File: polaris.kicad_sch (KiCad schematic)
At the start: 22 parts, among them J101 XT60-M, J102 Screw_Terminal_01x02, J103 Screw_Terminal_01x02, J104 Screw_Terminal_01x02, J105 Screw_Terminal_01x02, J106 Screw_Terminal_01x02, J107 Screw_Terminal_01x02, J108 Screw_Terminal_01x03, J109 Screw_Terminal_01x03, J110 Screw_Terminal_01x03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

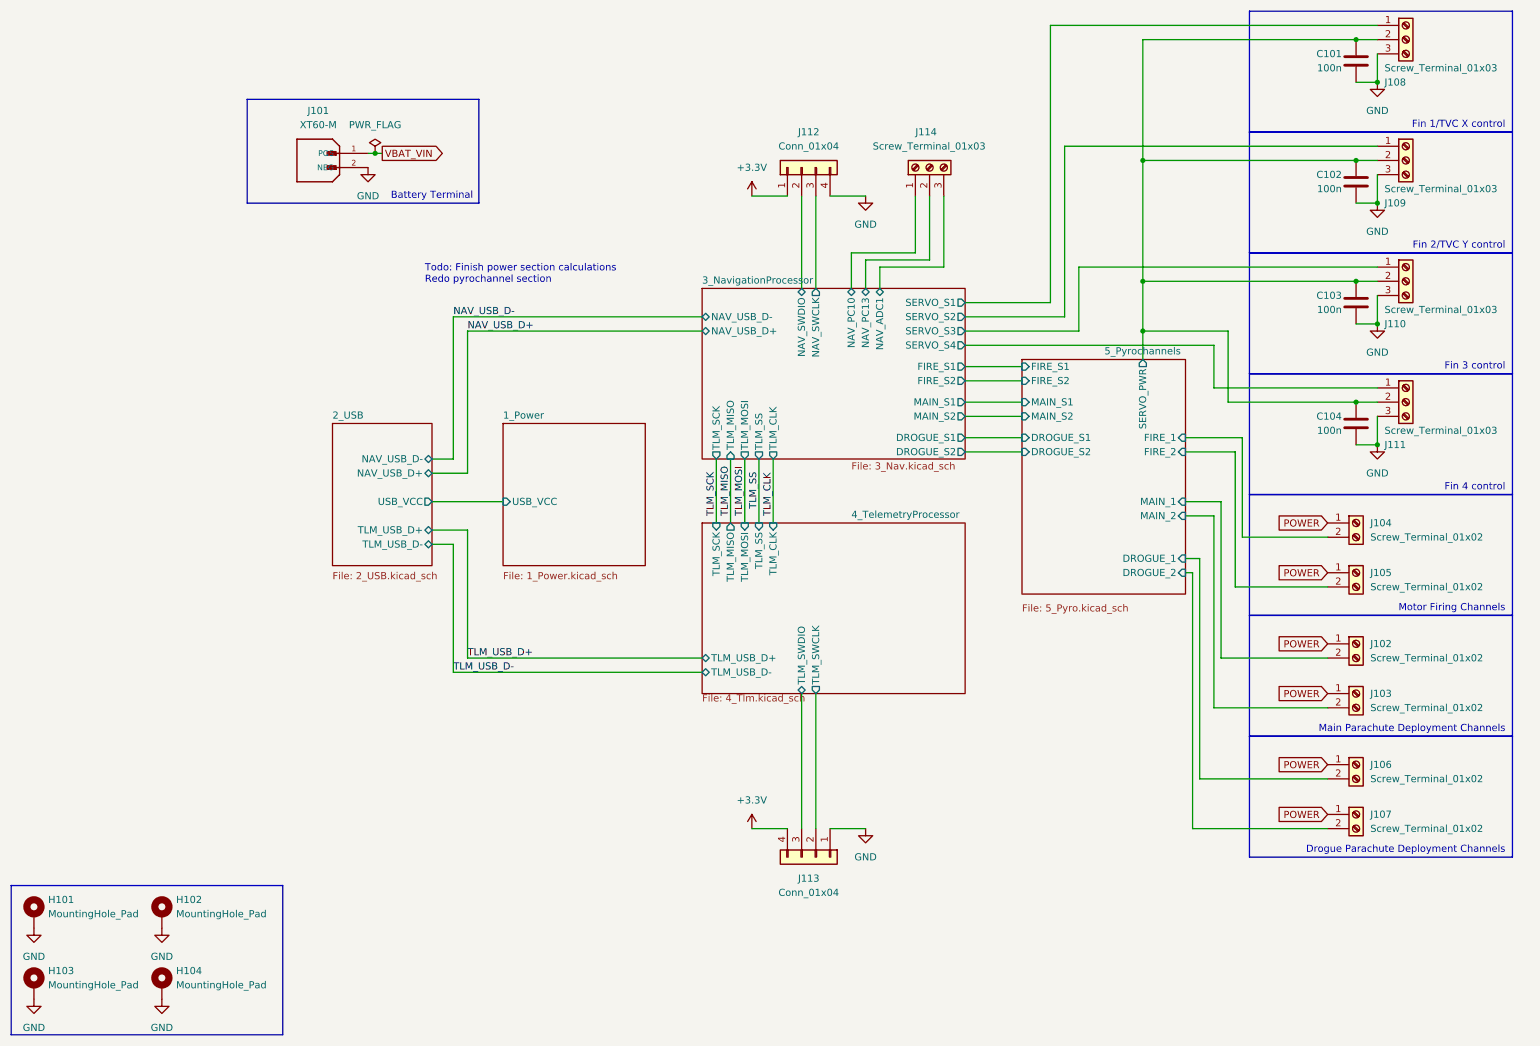
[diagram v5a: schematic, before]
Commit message: Renamed a few nets
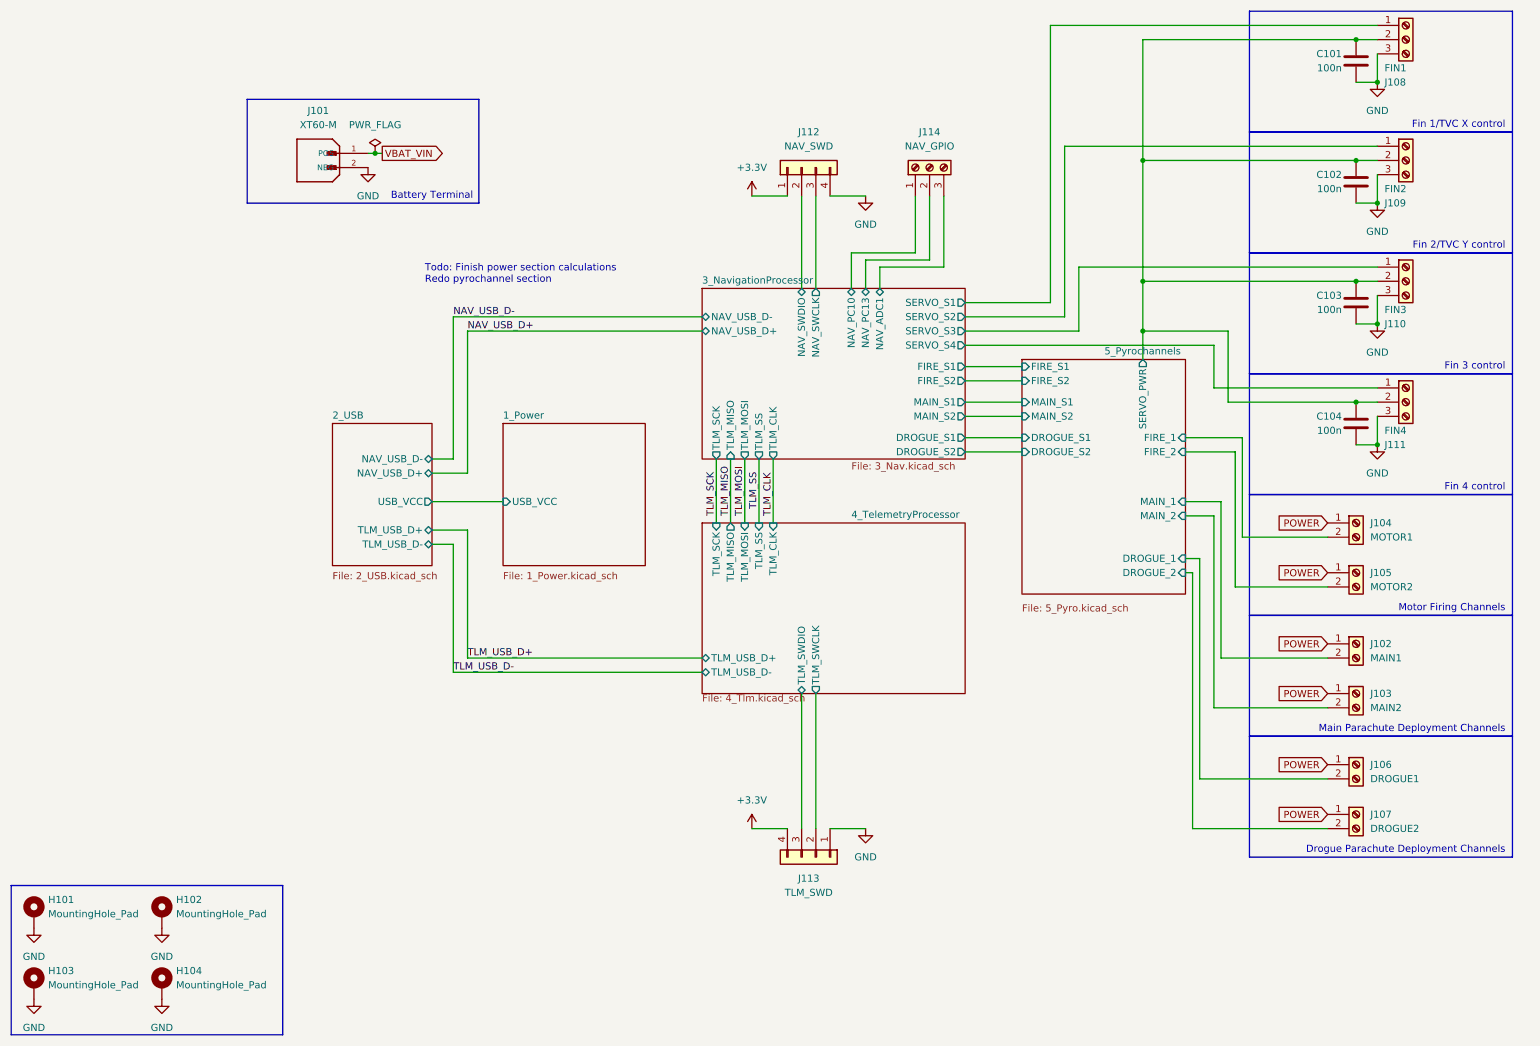
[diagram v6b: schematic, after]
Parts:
- J102: value Screw_Terminal_01x02 -> MAIN1
- J103: value Screw_Terminal_01x02 -> MAIN2
- J104: value Screw_Terminal_01x02 -> MOTOR1
- J105: value Screw_Terminal_01x02 -> MOTOR2
- J106: value Screw_Terminal_01x02 -> DROGUE1
- J107: value Screw_Terminal_01x02 -> DROGUE2
- J108: value Screw_Terminal_01x03 -> FIN1
- J109: value Screw_Terminal_01x03 -> FIN2
- J110: value Screw_Terminal_01x03 -> FIN3
- J111: value Screw_Terminal_01x03 -> FIN4
- J112: value Conn_01x04 -> NAV_SWD
- J113: value Conn_01x04 -> TLM_SWD
- J114: value Screw_Terminal_01x03 -> NAV_GPIO
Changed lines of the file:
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@@
 			)
 		)
-		(property "Value" "Screw_Terminal_01x03"
+		(property "Value" "FIN2"
 			(at 259.08 45.72 0)
 			(show_name no)
@@
 			)
 		)
-		(property "Value" "Screw_Terminal_01x02"
+		(property "Value" "DROGUE2"
 			(at 256.54 160.0199 0)
 			(show_name no)
@@
 			)
 		)
-		(property "Value" "Screw_Terminal_01x03"
+		(property "Value" "FIN3"
 			(at 259.08 67.31 0)
 			(show_name no)
@@
 			)
 		)
-		(property "Value" "Conn_01x04"
+		(property "Value" "NAV_SWD"
 			(at 156.21 38.1 90)
 			(show_name no)
@@
 			)
 		)
-		(property "Value" "Screw_Terminal_01x03"
+		(property "Value" "FIN1"
 			(at 259.08 24.13 0)
 			(show_name no)
@@
 			)
 		)
-		(property "Value" "Screw_Terminal_01x03"
+		(property "Value" "FIN4"
 			(at 259.08 88.9 0)
 			(show_name no)
@@
 		(dnp no)
 		(property "Reference" "J114"
-			(at 175.26 35.56 90)
+			(at 177.8 35.56 90)
 			(show_name no)
 			(do_not_autoplace no)
@@
 					(size 1.27 1.27)
 				)
-				(justify right)
 			)
 		)
-		(property "Value" "Screw_Terminal_01x03"
-			(at 167.64 38.1 90)
+		(property "Value" "NAV_GPIO"
+			(at 177.8 38.1 90)
 			(show_name no)
 			(do_not_autoplace no)
@@
 					(size 1.27 1.27)
 				)
-				(justify right)
 			)
 		)
@@
 			)
 		)
-		(property "Value" "Screw_Terminal_01x02"
+		(property "Value" "MOTOR2"
 			(at 256.54 116.8399 0)
 			(show_name no)
@@
 			)
 		)
-		(property "Value" "Screw_Terminal_01x02"
+		(property "Value" "MOTOR1"
 			(at 256.54 107.9499 0)
 			(show_name no)
@@
 			)
 		)
-		(property "Value" "Screw_Terminal_01x02"
+		(property "Value" "DROGUE1"
 			(at 256.54 151.1299 0)
 			(show_name no)
@@
 			)
 		)
-		(property "Value" "Conn_01x04"
+		(property "Value" "TLM_SWD"
 			(at 156.21 171.45 90)
 			(show_name no)
@@
 			)
 		)
-		(property "Value" "Screw_Terminal_01x02"
+		(property "Value" "MAIN1"
 			(at 256.54 129.5399 0)
 			(show_name no)
@@
 			)
 		)
-		(property "Value" "Screw_Terminal_01x02"
+		(property "Value" "MAIN2"
 			(at 256.54 138.43 0)
 			(show_name no)

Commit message: Redesigned the whole thing for the hundredth time
Changed from dual MCU to single MCU
Changed main MCU to STM32F446VE
Added CubeMX project (ioc) file for easy access to pinouts
Note: The PCB file still contains the previous connections and footprints
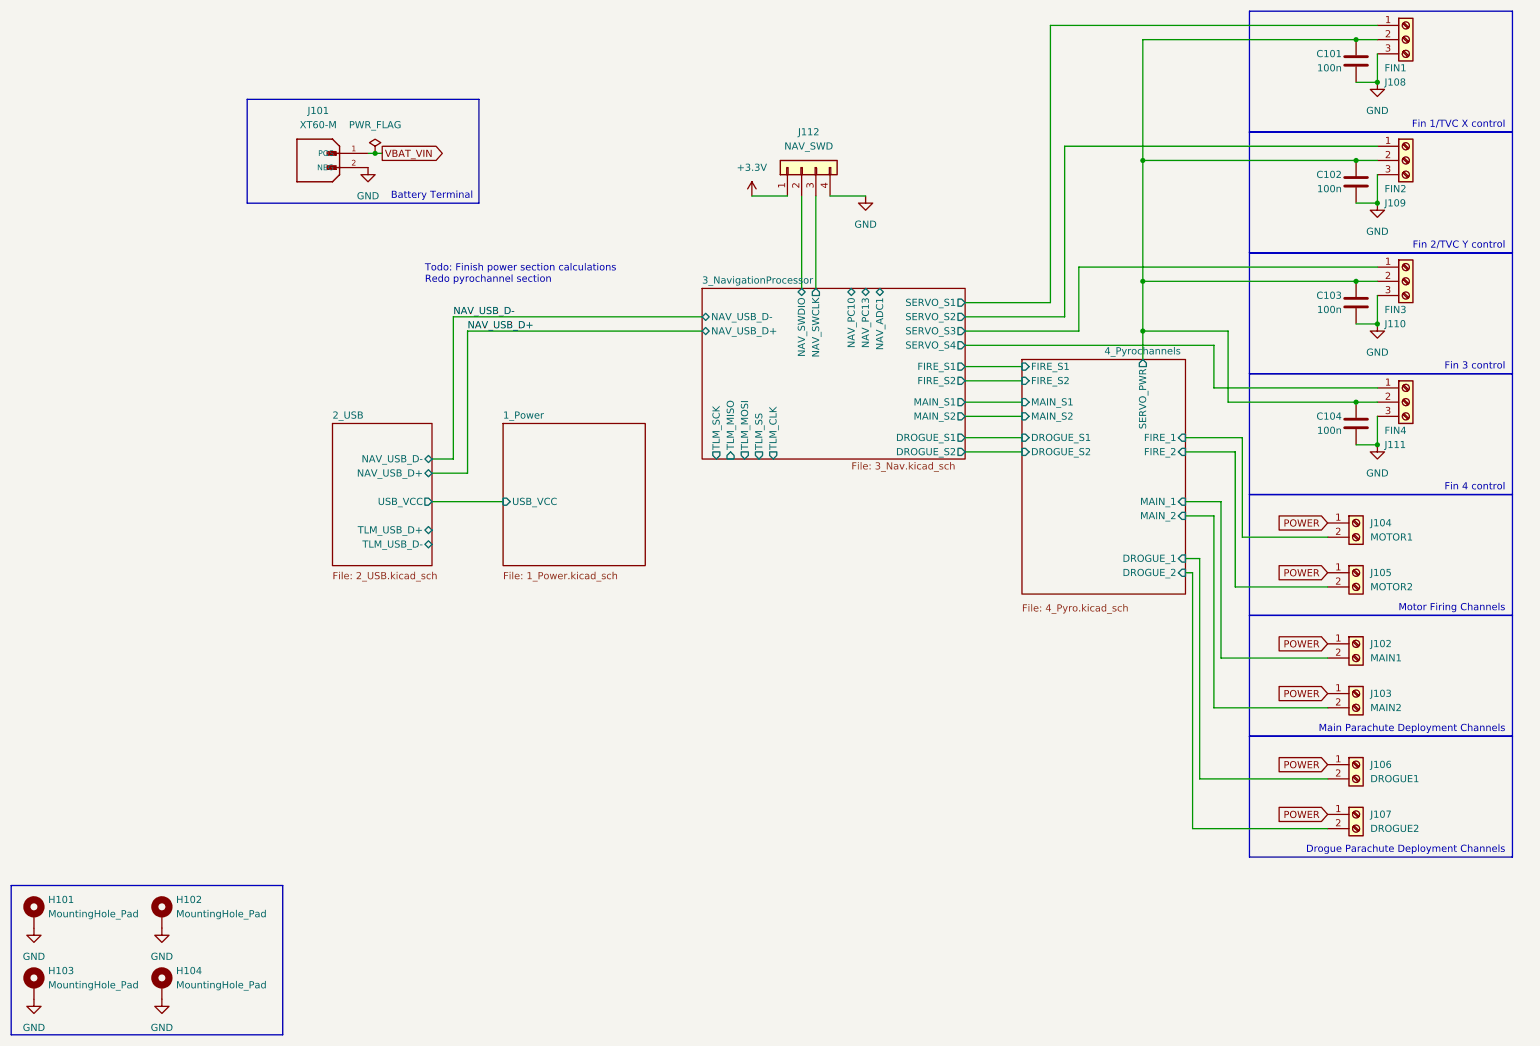
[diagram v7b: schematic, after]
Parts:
- removed J113: TLM_SWD, Connector_PinHeader_2.00mm:PinHeader_1x04_P2.00mm_Vertical, symbol Connector_Generic:Conn_01x04
- removed J114: NAV_GPIO, TerminalBlock:TerminalBlock_Xinya_XY308-2.54-3P_1x03_P2.54mm_Horizontal, symbol Connector:Screw_Terminal_01x03
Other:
- sheet 5_Pyrochannels renamed 4_Pyrochannels
- removed sheet 4_TelemetryProcessor
- sheet 4_Pyrochannels: file 5_Pyro.kicad_sch -> 4_Pyro.kicad_sch

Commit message: Continued connections for the new NAV
Added continuity sensing through a 8:1 mux
Restructured schematic so that everything actually fits in page 4
Updated CubeMX (ioc) file with pinout
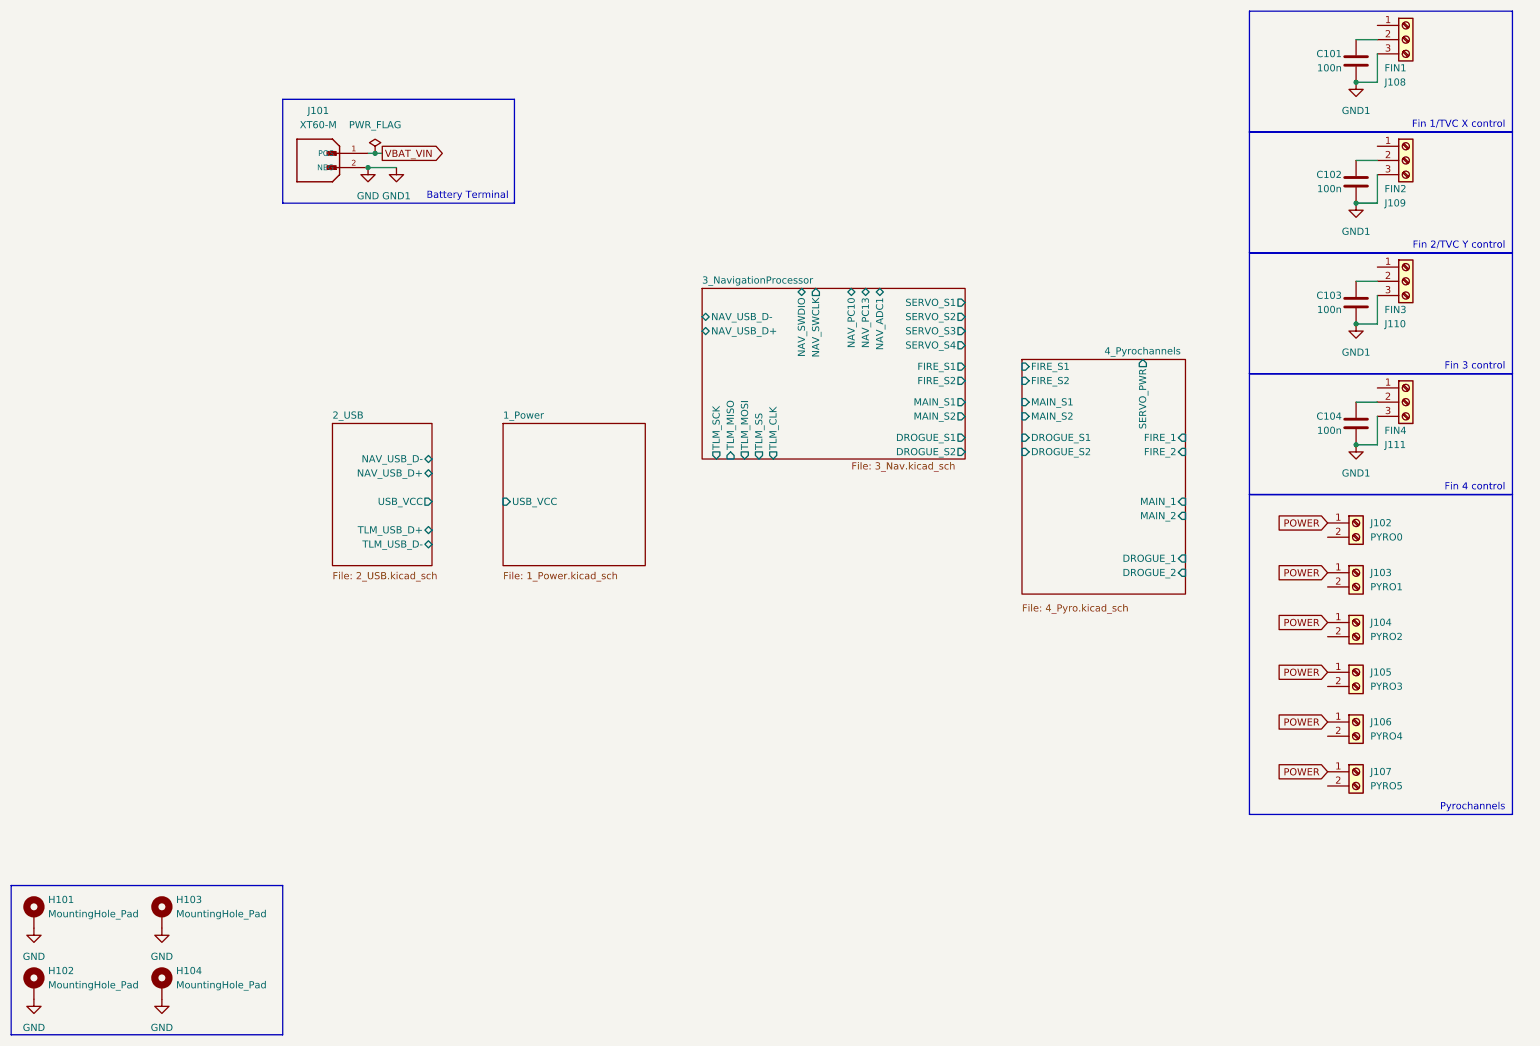
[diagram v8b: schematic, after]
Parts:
- removed J112: NAV_SWD, Connector_PinHeader_2.00mm:PinHeader_1x04_P2.00mm_Vertical, symbol Connector_Generic:Conn_01x04
- J102: renamed from J104; value MOTOR1 -> PYRO0
- J103: renamed from J105; value MOTOR2 -> PYRO1
- J104: renamed from J102; value MAIN1 -> PYRO2
- J105: renamed from J103; value MAIN2 -> PYRO3
- J106: value DROGUE1 -> PYRO4
- J107: value DROGUE2 -> PYRO5
- renumbered H103 to H102, H102 to H103
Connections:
- net 3_NavigationProcessor/SERVO_S1: no longer J108.1 (Pin_1)
- net 3_NavigationProcessor/SERVO_S2: no longer J109.1 (Pin_1)
- net 3_NavigationProcessor/SERVO_S3: no longer J110.1 (Pin_1)
- net 3_NavigationProcessor/SERVO_S4: no longer J111.1 (Pin_1)
- net 4_Pyrochannels/DROGUE_1: no longer J106.2 (Pin_2)
- net 4_Pyrochannels/DROGUE_2: no longer J107.2 (Pin_2)
- net 4_Pyrochannels/FIRE_1: no longer J102.2 (Pin_2)
- net 4_Pyrochannels/FIRE_2: no longer J103.2 (Pin_2)
- net 4_Pyrochannels/MAIN_1: no longer J104.2 (Pin_2)
- net 4_Pyrochannels/MAIN_2: no longer J105.2 (Pin_2)
- net 4_Pyrochannels/SERVO_PWR: no longer C101.1, C102.1, C103.1, C104.1, J108.2 (Pin_2), J109.2 (Pin_2), J110.2 (Pin_2), J111.2 (Pin_2)
- new net: C102.1, J109.2 (Pin_2)
- new net: C103.1, J110.2 (Pin_2)
- new net: C101.1, J108.2 (Pin_2)
- new net: C104.1, J111.2 (Pin_2)
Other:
- note added: "Pyrochannels"
- note removed: "Drogue Parachute Deployment Channels"
- note removed: "Main Parachute Deployment Channels"
- note removed: "Motor Firing Channels"
- note removed: "Todo: Finish power section calculations Redo pyrochannel section"
- moved on the sheet: J104, J105, J106, J107
